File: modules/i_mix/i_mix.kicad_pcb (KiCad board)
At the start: 2 copper layers, 30.5 x 68.6 mm, 4 parts

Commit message: Add production files
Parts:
- added C1: 0.1uf, Capacitor_SMD:C_0402_1005Metric, F.Cu at (69.2, 53.8)
- added C2: 0.1uf, Capacitor_SMD:C_0402_1005Metric, F.Cu at (60.0, 54.1)
- added C3: 100uf, Capacitor_SMD:C_1206_3216Metric, F.Cu at (50.3, 101.0)
- added C4: 0.1uf, Capacitor_SMD:C_0402_1005Metric, F.Cu at (69.3, 99.7)
- added R1: 1k, Resistor_SMD:R_0402_1005Metric, F.Cu at (60.6, 101.5)
- added R10: 200k, Resistor_SMD:R_0402_1005Metric, F.Cu at (63.6, 77.5)
- added R11: 200k, Resistor_SMD:R_0402_1005Metric, F.Cu at (71.2, 94.6)
- added R12: 1k, Resistor_SMD:R_0402_1005Metric, F.Cu at (74.4, 94.6)
- added R2: 1k, Resistor_SMD:R_0402_1005Metric, F.Cu at (63.9, 101.5)
- added R3: 1M, Resistor_SMD:R_0402_1005Metric, F.Cu at (72.4, 58.7)
- added R4: 200k, Resistor_SMD:R_0402_1005Metric, F.Cu at (60.8, 93.6)
- added R5: 1M, Resistor_SMD:R_0402_1005Metric, F.Cu at (72.4, 60.1)
- added R6: 200k, Resistor_SMD:R_0402_1005Metric, F.Cu at (64.0, 93.6)
- added R7: 1M, Resistor_SMD:R_0402_1005Metric, F.Cu at (51.3, 58.4)
- added R8: 200k, Resistor_SMD:R_0402_1005Metric, F.Cu at (60.6, 77.5)
- added R9: 1M, Resistor_SMD:R_0402_1005Metric, F.Cu at (51.3, 60.3)
- added RV1: 50k, BreadModular_Pots:Potentiometer_RV09, F.Cu at (55.4, 66.7)
- added RV2: 50k, BreadModular_Pots:Potentiometer_RV09, F.Cu at (69.3, 66.7)
- added RV3: 50k, BreadModular_Pots:Potentiometer_RV09, F.Cu at (55.4, 83.8)
- added RV4: 50k, BreadModular_Pots:Potentiometer_RV09, F.Cu at (69.3, 83.8)
- added U1: MCP6002-xSN, Package_SO:SOIC-8-1EP_3.9x4.9mm_P1.27mm_EP2.29x3mm, F.Cu at (57.8, 57.3)
- added U2: MCP6002-xSN, Package_SO:SOIC-8-1EP_3.9x4.9mm_P1.27mm_EP2.29x3mm, F.Cu at (66.6, 57.3)
- added U3: MCP6002-xSN, Package_SO:SOIC-8-1EP_3.9x4.9mm_P1.27mm_EP2.29x3mm, F.Cu at (72.9, 100.3)
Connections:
- INPUT1 pad 1: unconnected-(INPUT1-Pin_1-Pad1) -> IN_1
- INPUT1 pad 2: unconnected-(INPUT1-Pin_2-Pad2) -> IN_2
- INPUT1 pad 3: unconnected-(INPUT1-Pin_3-Pad3) -> IN_3
- INPUT1 pad 4: unconnected-(INPUT1-Pin_4-Pad4) -> IN_4
- OUTPUT1 pad 1: unconnected-(OUTPUT1-Pin_1-Pad1) -> MIXOUT
- OUTPUT1 pad 2: unconnected-(OUTPUT1-Pin_2-Pad2) -> MIXOUT
- OUTPUT1 pad 3: unconnected-(OUTPUT1-Pin_3-Pad3) -> MIXOUT
- OUTPUT1 pad 4: unconnected-(OUTPUT1-Pin_4-Pad4) -> MIXOUT
- OUTPUT1 pad 5: unconnected-(OUTPUT1-Pin_5-Pad5) -> MIXOUT
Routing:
- net V_MID: track 0.00 -> 224.3 mm, vias 0 -> 5
- net GND: track 10.2 -> 160.5 mm, vias 0 -> 6
- net V_SUPPLY: track 10.2 -> 109.8 mm, vias 0 -> 5
- net MIXOUT: track 0.00 -> 50.9 mm
- net Net-(U2A--): track 0.00 -> 48.1 mm, vias 0 -> 2
- net IN_4: track 0.00 -> 43.8 mm, vias 0 -> 2
- net Net-(U2B--): track 0.00 -> 37.6 mm, vias 0 -> 2
- net IN_3: track 0.00 -> 36.5 mm, vias 0 -> 4
- net Net-(U3A--): track 0.00 -> 33.7 mm
- net Net-(U1A--): track 0.00 -> 32.7 mm
- net Net-(U1B--): track 0.00 -> 27.2 mm, vias 0 -> 2
- net IN_2: track 0.00 -> 26.4 mm
- net IN_1: track 0.00 -> 18.8 mm
- net Net-(R6-Pad1): track 0.00 -> 7.04 mm
- net Net-(R10-Pad1): track 0.00 -> 6.65 mm
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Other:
- board text added: "1"
- board text added: "2"
- board text added: "3"
- board text added: "4"
- board text added: "I_MIX"
- board text added: "I_MIX 0.1.0"
- board text added: "MIXOUT"
- board text removed: "NAME"
- board text removed: "NAME 0.0.0"

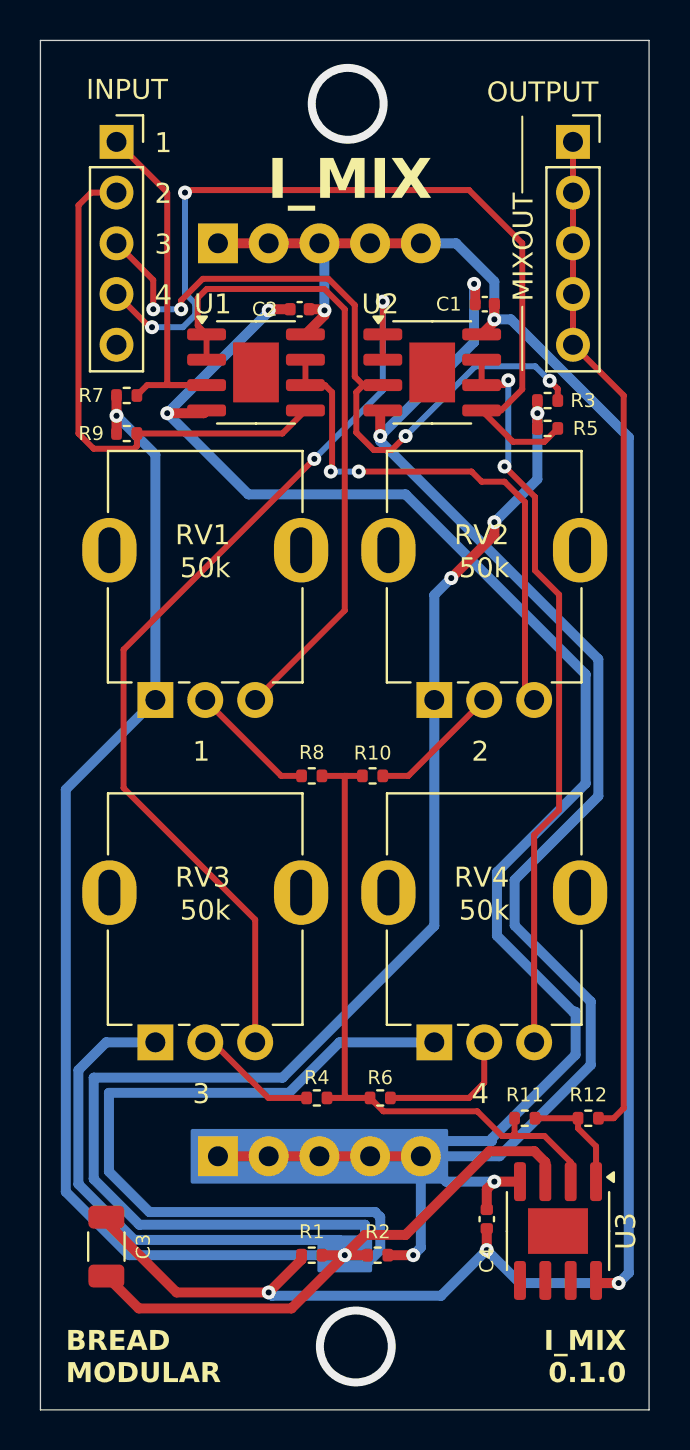
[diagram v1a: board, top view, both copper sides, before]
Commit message: i_mix: Use inverting buffers This will reducing picking up noise coming from cables
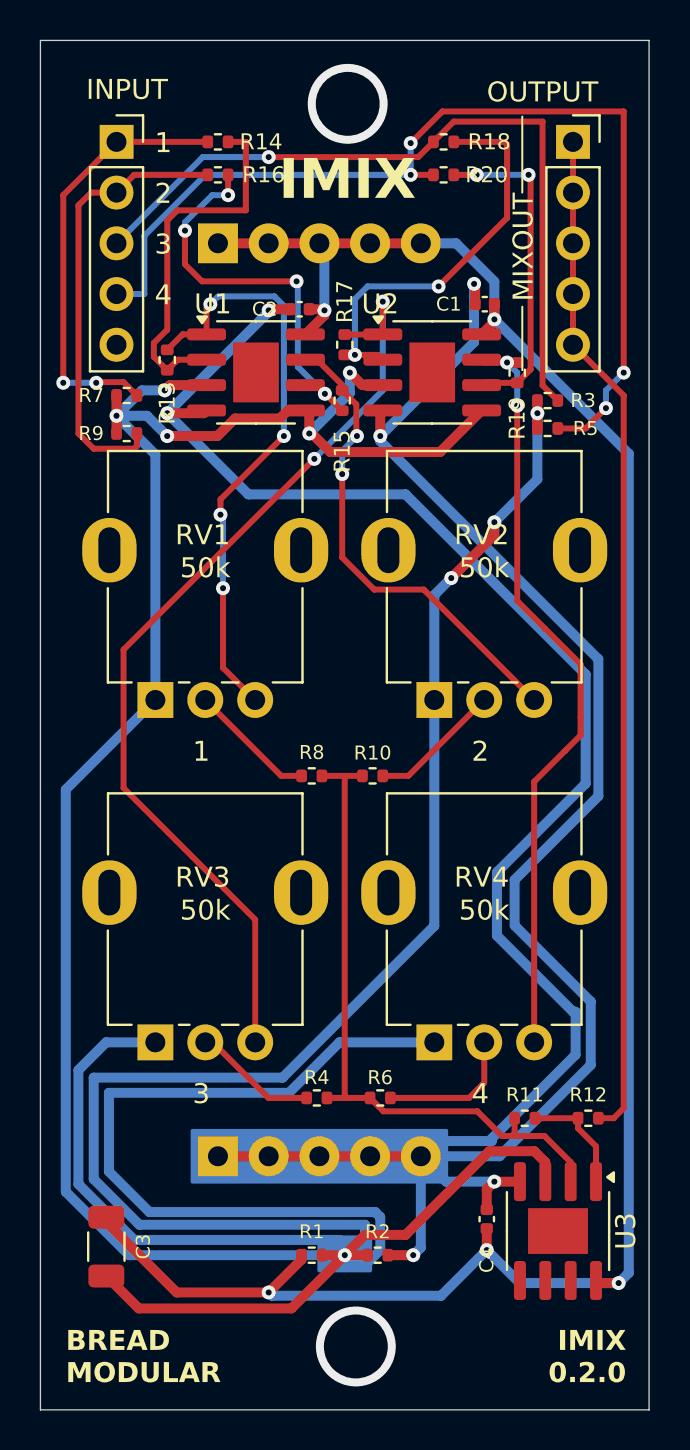
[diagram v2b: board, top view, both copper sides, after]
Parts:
- added R13: 100k, Resistor_SMD:R_0402_1005Metric, F.Cu at (53.3, 56.6)
- added R14: 100k, Resistor_SMD:R_0402_1005Metric, F.Cu at (55.9, 45.7)
- added R15: 100k, Resistor_SMD:R_0402_1005Metric, F.Cu at (62.1, 58.7)
- added R16: 100k, Resistor_SMD:R_0402_1005Metric, F.Cu at (55.9, 47.4)
- added R17: 100k, Resistor_SMD:R_0402_1005Metric, F.Cu at (62.2, 55.9)
- added R18: 100k, Resistor_SMD:R_0402_1005Metric, F.Cu at (67.2, 45.7)
- added R19: 100k, Resistor_SMD:R_0402_1005Metric, F.Cu at (70.9, 57.3)
- added R20: 100k, Resistor_SMD:R_0402_1005Metric, F.Cu at (67.2, 47.4)
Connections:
- RV1 pad 3: Net-(U1A--) -> Net-(R13-Pad2)
- RV2 pad 3: Net-(U1B--) -> Net-(R15-Pad2)
- RV3 pad 3: Net-(U2A--) -> Net-(R17-Pad2)
- RV4 pad 3: Net-(U2B--) -> Net-(R19-Pad2)
- U1 pad 1: Net-(U1A--) -> Net-(R13-Pad2)
- U1 pad 3: IN_1 -> V_MID
- U1 pad 5: IN_2 -> V_MID
- U1 pad 7: Net-(U1B--) -> Net-(R15-Pad2)
- U2 pad 1: Net-(U2A--) -> Net-(R17-Pad2)
- U2 pad 3: IN_3 -> V_MID
- U2 pad 5: IN_4 -> V_MID
- U2 pad 7: Net-(U2B--) -> Net-(R19-Pad2)
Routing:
- net Net-(R17-Pad2): track 0.00 -> 48.7 mm, vias 0 -> 2
- net Net-(R19-Pad2): track 0.00 -> 38.4 mm, vias 0 -> 2
- net V_MID: track 224.3 -> 256.7 mm, vias 5 -> 9
- net Net-(R13-Pad2): track 0.00 -> 29.7 mm, vias 0 -> 4
- net Net-(U2A--): track 48.1 -> 20.5 mm
- net Net-(R15-Pad2): track 0.00 -> 24.2 mm, vias 0 -> 2
- net Net-(U2B--): track 37.6 -> 16.3 mm
- net Net-(U1A--): track 32.7 -> 19.2 mm
- net IN_4: track 43.8 -> 51.0 mm, vias 2 -> 4
- net Net-(U1B--): track 27.2 -> 20.4 mm, vias 2 -> 4
- net IN_2: track 26.4 -> 22.5 mm
- net IN_1: track 18.8 -> 21.7 mm, vias 0 -> 2
- net IN_3: track 36.5 -> 38.1 mm, vias 4 -> 1
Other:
- board text added: "IMIX"
- board text added: "IMIX 0.2.0"
- board text removed: "I_MIX"
- board text removed: "I_MIX 0.1.0"
